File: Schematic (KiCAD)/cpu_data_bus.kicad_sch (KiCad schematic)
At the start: 149 parts, among them P13 INVERT, P19 INVERT, P26 INVERT, P5 INVERT, P7 INVERT, X18 INVERT, X19 INVERT, X20 INVERT, X21 INVERT, X22 INVERT, X23 INVERT, X24 INVERT, X25 INVERT, Y11 INVERT, Y12 INVERT, Y18 INVERT, Y19 INVERT, Y25 INVERT, Y26 INVERT, Y4 INVERT, Y5 INVERT

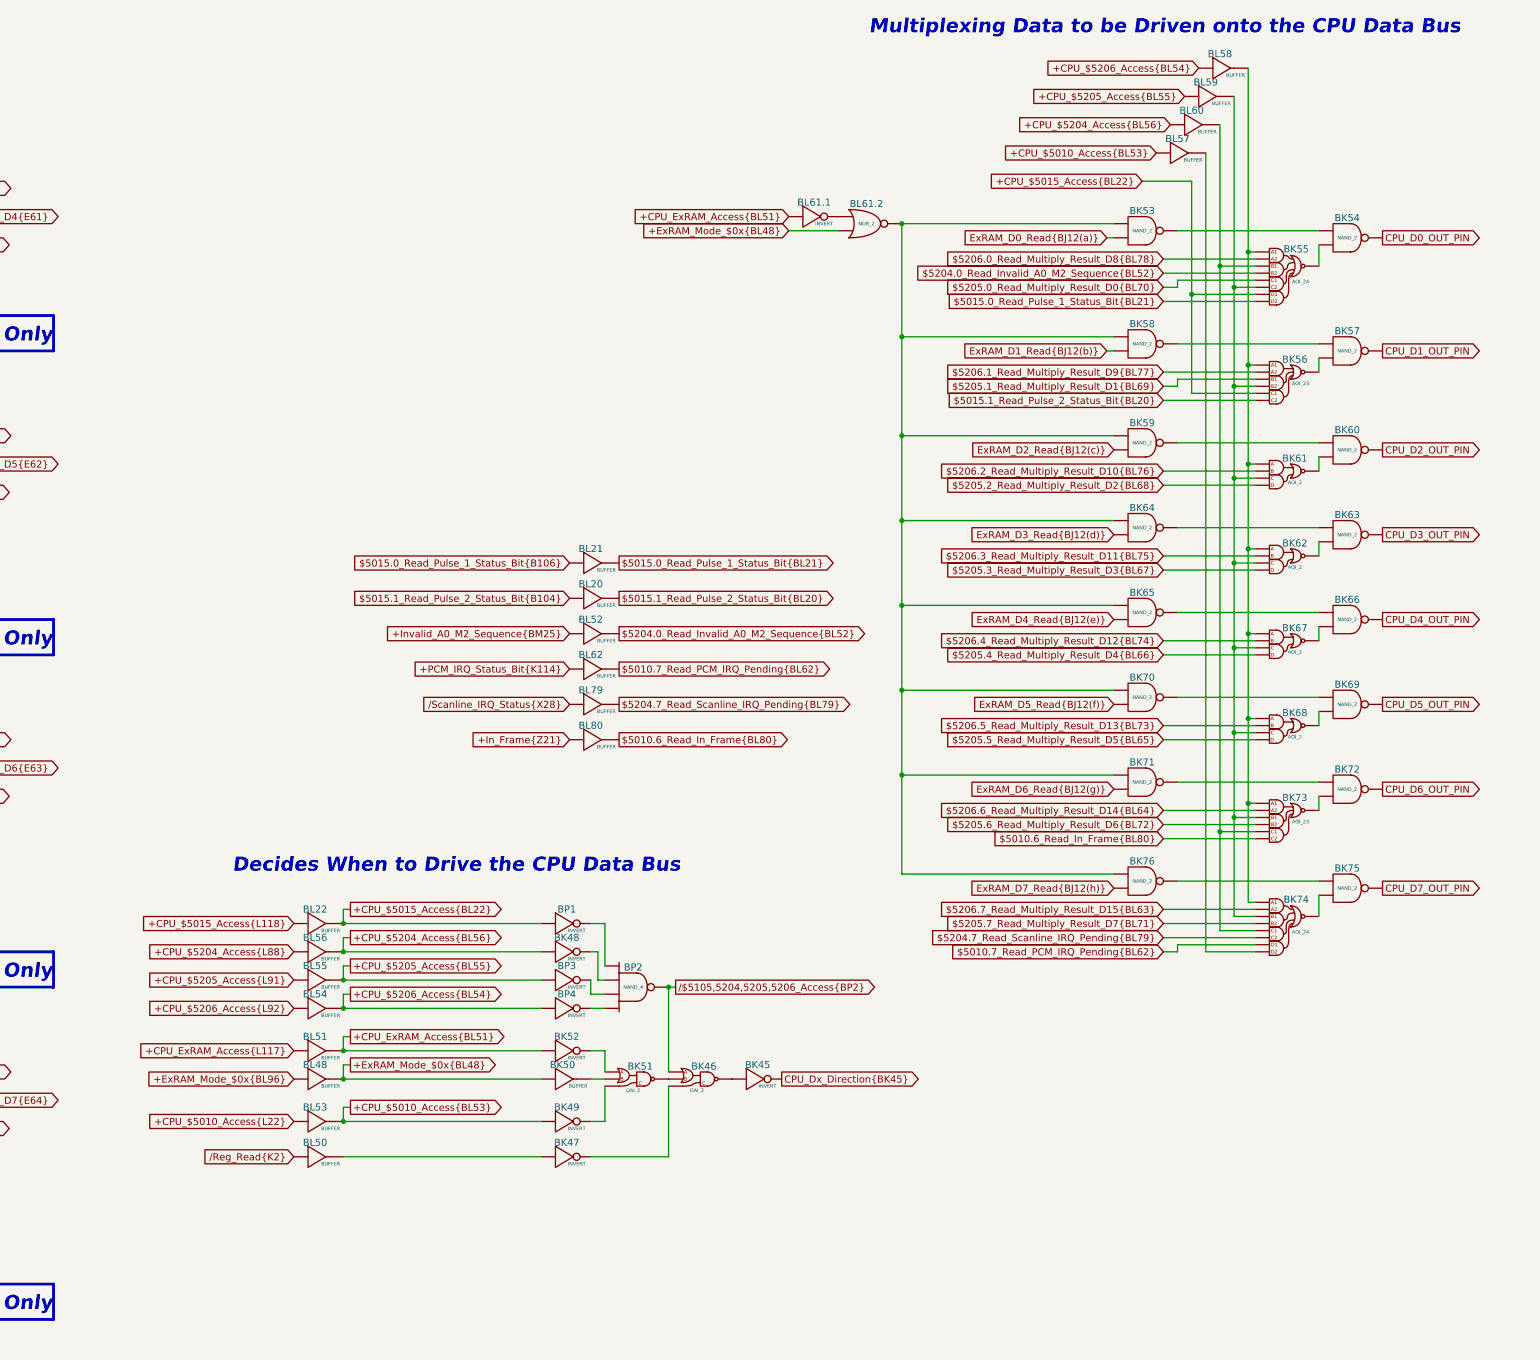
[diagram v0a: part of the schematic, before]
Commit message: Added the new MMC5A read-register bits in the schematic. Additional MMC5A tracing work.
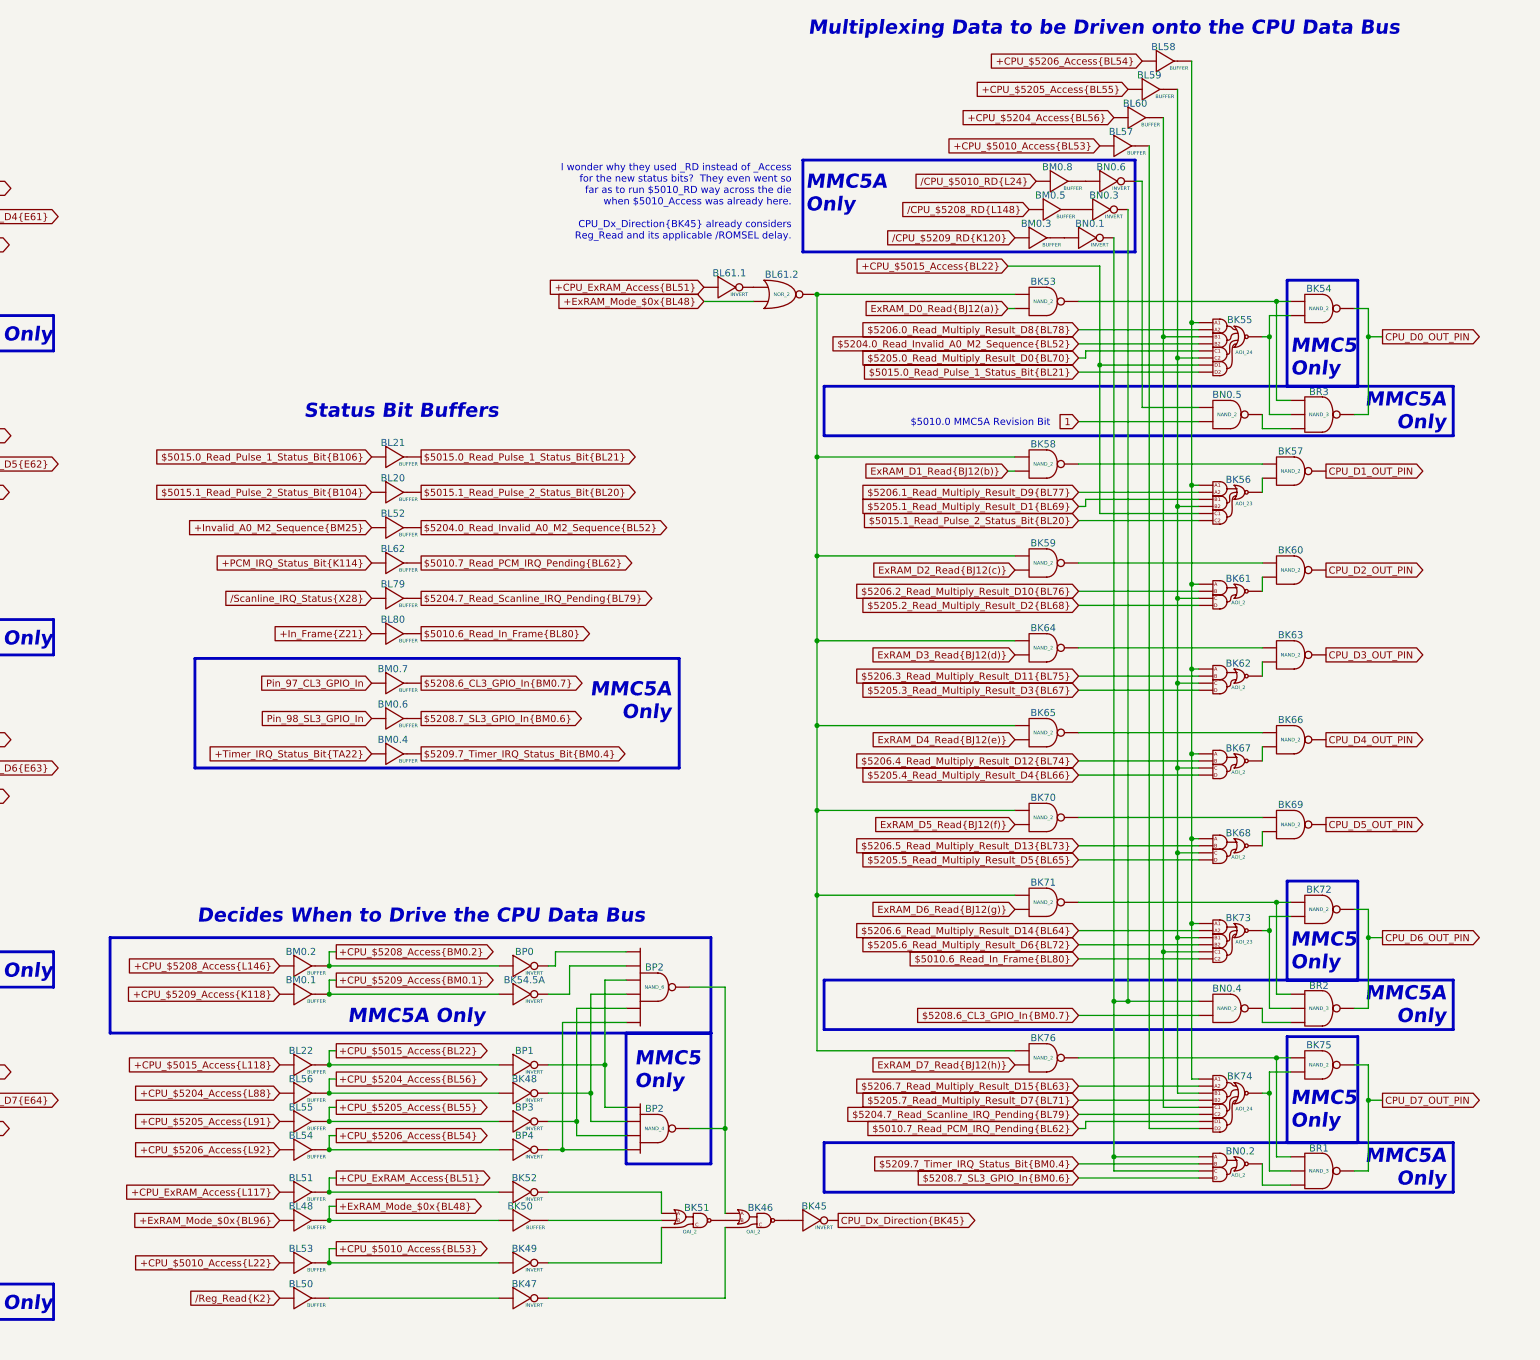
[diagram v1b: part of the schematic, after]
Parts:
- added BK54.5A, BN0.1, BN0.3, BN0.6, BP0: INVERT, symbol MMC5:INVERT
- added BM0.1, BM0.2, BM0.3, BM0.4, BM0.5, BM0.6, BM0.7, BM0.8: BUFFER, symbol MMC5:BUFFER
- added BN0.2: AOI_2, symbol MMC5:AOI_2
- added BN0.4, BN0.5: NAND_2, symbol MMC5:NAND_2
- added BP2: NAND_6, symbol MMC5:NAND_6
- added BR1, BR2, BR3: NAND_3, symbol MMC5:NAND_3
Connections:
- net CPU_D0_OUT_PIN: now also BR3. (X)
- net CPU_D6_OUT_PIN: now also BR2. (X)
- net CPU_D7_OUT_PIN: now also BR1. (X)
- net at BK47. (X): now also BK46. (X); no longer BL50. (X)
- net at BK46. (X): now also BK45. (X); no longer BK47. (X)
- net at BP2. (X): now also BP4. (X), BP2. (X); no longer BK48. (X)
- net at BK51. (X): now also BK49. (X); no longer BK52. (X)
- removed net /$5105,5204,5205,5206_Access{BP2}: BK46. (X), BP2. (X)
- new net: BK55. (X), BK56. (X), BK61. (X), BK62. (X), BK67. (X), BK68. (X), BK73. (X), BK74. (X), BL58. (X)
- new net: BK55. (X), BK56. (X), BK61. (X), BK62. (X), BK67. (X), BK68. (X), BK73. (X), BK74. (X), BL59. (X)
- new net: BK66. (X), BK67. (X)
- new net: BK53. (X), BK58. (X), BK59. (X), BK64. (X), BK65. (X), BK70. (X), BK71. (X), BK76. (X), BL61.2. (X)
- new net: BK63. (X), BK64. (X)
- new net: BK69. (X), BK70. (X)
- new net: BK68. (X), BK69. (X)
- new net: BK65. (X), BK66. (X)
- new net: BN0.1. (X), BN0.2. (X), BN0.3. (X), BN0.4. (X)
- new net: BM0.3. (X), BN0.1. (X)
- new net: BL61.1. (X), BL61.2. (X)
- new net: BK57. (X), BK58. (X)
- new net: G15. (X), G16. (X)
- new net: BK75. (X), BK76. (X), BR1. (X)
- new net: G10. (X), G9. (X)
- new net: AE15. (X), AE19. (X), G13. (X), MUL20. (X), TF2. (X), X19. (X)
- new net: BK47. (X), BL50. (X)
- new net: G1. (X), G2. (X)
- new net: BM0.5. (X), BN0.3. (X)
- new net: BM0.8. (X), BN0.6. (X)
- new net: G7. (X), G8. (X)
- new net: G11. (X), G12. (X)
- new net: G5. (X), G6. (X)
- new net: BK53. (X), BK54. (X), BR3. (X)
- new net: G3. (X), G4. (X)
- new net: BK48. (X), BP2. (X), BP2. (X)
- new net: BP2. (X), BP2. (X), BP3. (X)
- new net: BK55. (X), BK73. (X), BK74. (X), BL60. (X)
- new net: BK54. (X), BK55. (X), BR3. (X)
- new net: BK72. (X), BK73. (X), BR2. (X)
- new net: BK71. (X), BK72. (X), BR2. (X)
- new net: BK74. (X), BK75. (X), BR1. (X)
- new net: BK74. (X), BL57. (X)
- new net: BK60. (X), BK61. (X)
- new net: BK59. (X), BK60. (X)
- new net: BN0.2. (X), BR1. (X)
- new net: BN0.5. (X), BN0.6. (X)
- new net: BN0.5. (X), BR3. (X)
- new net: BK56. (X), BK57. (X)
- new net: BN0.4. (X), BR2. (X)
- new net: BP1. (X), BP2. (X), BP2. (X)
- new net: BK54.5A. (X), BP2. (X)
- new net: BK46. (X), BP2. (X), BP2. (X)
- new net: BP0. (X), BP2. (X)
- new net: BK62. (X), BK63. (X)
- new net: BK51. (X), BK52. (X)
- new net: BK50. (X), BK51. (X)
- new net: BK46. (X), BK51. (X)
- new net $5208.6_CL3_GPIO_In{BM0.7}: BM0.7. (X), BN0.4. (X)
- new net $5208.7_SL3_GPIO_In{BM0.6}: BM0.6. (X), BN0.2. (X)
- new net $5209.7_Timer_IRQ_Status_Bit{BM0.4}: BM0.4. (X), BN0.2. (X)
- new net +CPU_$5208_Access{BM0.2}: BM0.2. (X), BP0. (X)
- new net +CPU_$5208_Access{L146}: BM0.2. (X)
- new net +CPU_$5209_Access{BM0.1}: BK54.5A. (X), BM0.1. (X)
- new net +CPU_$5209_Access{K118}: BM0.1. (X)
- new net +Timer_IRQ_Status_Bit{TA22}: BM0.4. (X)
- new net 1: BN0.5. (X)
- new net Pin_97_CL3_GPIO_In: BM0.7. (X)
- new net Pin_98_SL3_GPIO_In: BM0.6. (X)
- new net /CPU_$5010_RD{L24}: BM0.8. (X)
- new net /CPU_$5208_RD{L148}: BM0.5. (X)
- new net /CPU_$5209_RD{K120}: BM0.3. (X)
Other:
- note added: "$5010.0 MMC5A Revision Bit"
- note added: "I wonder why they used _RD instead of _Access for the new status bits? They even went so far as to run $5010_RD way across the die when $5010_Access was already here. CPU_Dx_Direction{BK45} already considers Reg_Read and its applicable /ROMSEL delay."
- note added: "MMC5 Only"
- note added: "Status Bit Buffers"
- moved on the sheet: BK45, BK46, BK47, BK48, BK49, BK50, BK51, BK52, BK53, BK54, BK55, BK56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

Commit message: - Fixed the register read bit schematic errors noted by Joe in the Nesdev forum.
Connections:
- net at BN0.1. (X): now also BN0.2. (X); no longer BM0.3. (X)
- net at BK47. (X): now also BK46. (X); no longer BL50. (X)
- net at BK46. (X): now also BK45. (X); no longer BK47. (X)
- net at BN0.3. (X): now also BN0.2. (X), BN0.4. (X); no longer BM0.5. (X)
- net at BN0.6. (X): now also BN0.5. (X); no longer BM0.8. (X)
- net at BP2. (X): now also BP0. (X); no longer BK54.5A. (X)
- net at BK51. (X): now also BK49. (X); no longer BK52. (X)
- new net: BK55. (X), BK56. (X), BK61. (X), BK62. (X), BK67. (X), BK68. (X), BK73. (X), BK74. (X), BL58. (X)
- new net: BK55. (X), BK56. (X), BK61. (X), BK62. (X), BK67. (X), BK68. (X), BK73. (X), BK74. (X), BL59. (X)
- new net: BK66. (X), BK67. (X)
- new net: BK53. (X), BK58. (X), BK59. (X), BK64. (X), BK65. (X), BK70. (X), BK71. (X), BK76. (X), BL61.2. (X)
- new net: BK63. (X), BK64. (X)
- new net: BK69. (X), BK70. (X)
- new net: BK68. (X), BK69. (X)
- new net: BK65. (X), BK66. (X)
- new net: BM0.3. (X), BN0.1. (X)
- new net: BL61.1. (X), BL61.2. (X)
- new net: BK57. (X), BK58. (X)
- new net: G15. (X), G16. (X)
- new net: BK75. (X), BK76. (X), BR1. (X)
- new net: G10. (X), G9. (X)
- new net: AE15. (X), AE19. (X), G13. (X), MUL20. (X), TF2. (X), X19. (X)
- new net: BK47. (X), BL50. (X)
- new net: G1. (X), G2. (X)
- new net: BM0.5. (X), BN0.3. (X)
- new net: BM0.8. (X), BN0.6. (X)
- new net: G7. (X), G8. (X)
- new net: G11. (X), G12. (X)
- new net: G5. (X), G6. (X)
- new net: BK53. (X), BK54. (X), BR3. (X)
- new net: G3. (X), G4. (X)
- new net: BK48. (X), BP2. (X), BP2. (X)
- new net: BP2. (X), BP2. (X), BP3. (X)
- new net: BK55. (X), BK73. (X), BK74. (X), BL60. (X)
- new net: BK54. (X), BK55. (X), BR3. (X)
- new net: BK72. (X), BK73. (X), BR2. (X)
- new net: BK71. (X), BK72. (X), BR2. (X)
- new net: BK74. (X), BK75. (X), BR1. (X)
- new net: BK74. (X), BL57. (X)
- new net: BK60. (X), BK61. (X)
- new net: BK59. (X), BK60. (X)
- new net: BN0.2. (X), BR1. (X)
- new net: BN0.5. (X), BR3. (X)
- new net: BK56. (X), BK57. (X)
- new net: BN0.4. (X), BR2. (X)
- new net: BP1. (X), BP2. (X), BP2. (X)
- new net: BK54.5A. (X), BP2. (X)
- new net: BK46. (X), BP2. (X), BP2. (X)
- new net: BP2. (X), BP2. (X), BP4. (X)
- new net: BK62. (X), BK63. (X)
- new net: BK51. (X), BK52. (X)
- new net: BK50. (X), BK51. (X)
- new net: BK46. (X), BK51. (X)
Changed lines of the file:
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@@
 	)
 	(junction
-		(at 345.44 220.98)
-		(diameter 0)
-		(color 0 0 0 0)
-	)
-	(junction
 		(at 104.14 106.68)
 		(diameter 0)
@@
 	)
 	(junction
-		(at 345.44 193.04)
-		(diameter 0)
-		(color 0 0 0 0)
-	)
-	(junction
 		(at 359.41 118.11)
 		(diameter 0)
@@
 	(wire
 		(pts
-			(xy 345.44 193.04) (xy 345.44 220.98)
-		)
-		(stroke
-			(width 0)
-			(type default)
-		)
-	)
-	(wire
-		(pts
 			(xy 53.34 106.68) (xy 52.07 106.68)
 		)
@@
 	(wire
 		(pts
+			(xy 347.98 220.98) (xy 360.68 220.98)
+		)
+		(stroke
+			(width 0)
+			(type default)
+		)
+	)
+	(wire
+		(pts
 			(xy 34.29 231.14) (xy 34.29 241.3)
 		)
@@
 	(wire
 		(pts
-			(xy 345.44 220.98) (xy 345.44 223.52)
+			(xy 345.44 55.88) (xy 345.44 223.52)
 		)
 		(stroke
@@
 	(wire
 		(pts
-			(xy 345.44 220.98) (xy 360.68 220.98)
-		)
-		(stroke
-			(width 0)
-			(type default)
-		)
-	)
-	(wire
-		(pts
 			(xy 34.29 137.16) (xy 34.29 142.24)
 		)
@@
 	(wire
 		(pts
+			(xy 347.98 193.04) (xy 347.98 220.98)
+		)
+		(stroke
+			(width 0)
+			(type default)
+		)
+	)
+	(wire
+		(pts
 			(xy 391.16 176.53) (xy 391.16 181.61)
 		)
@@
 	(wire
 		(pts
-			(xy 345.44 55.88) (xy 345.44 193.04)
-		)
-		(stroke
-			(width 0)
-			(type default)
-		)
-	)
-	(wire
-		(pts
 			(xy 391.16 176.53) (xy 388.62 176.53)
 		)
@@
 		)
 		(stroke
-			(width 0)
-			(type default)
-		)
-	)
-	(wire
-		(pts
-			(xy 345.44 193.04) (xy 347.98 193.04)
-		)
-		(stroke
